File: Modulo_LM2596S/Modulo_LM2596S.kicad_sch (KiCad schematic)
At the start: 17 parts, among them J101 Conn_01x01_Female, J102 Conn_01x01_Female, J103 Conn_01x01_Female, J104 Conn_01x01_Female, U101 LM2596S-ADJ

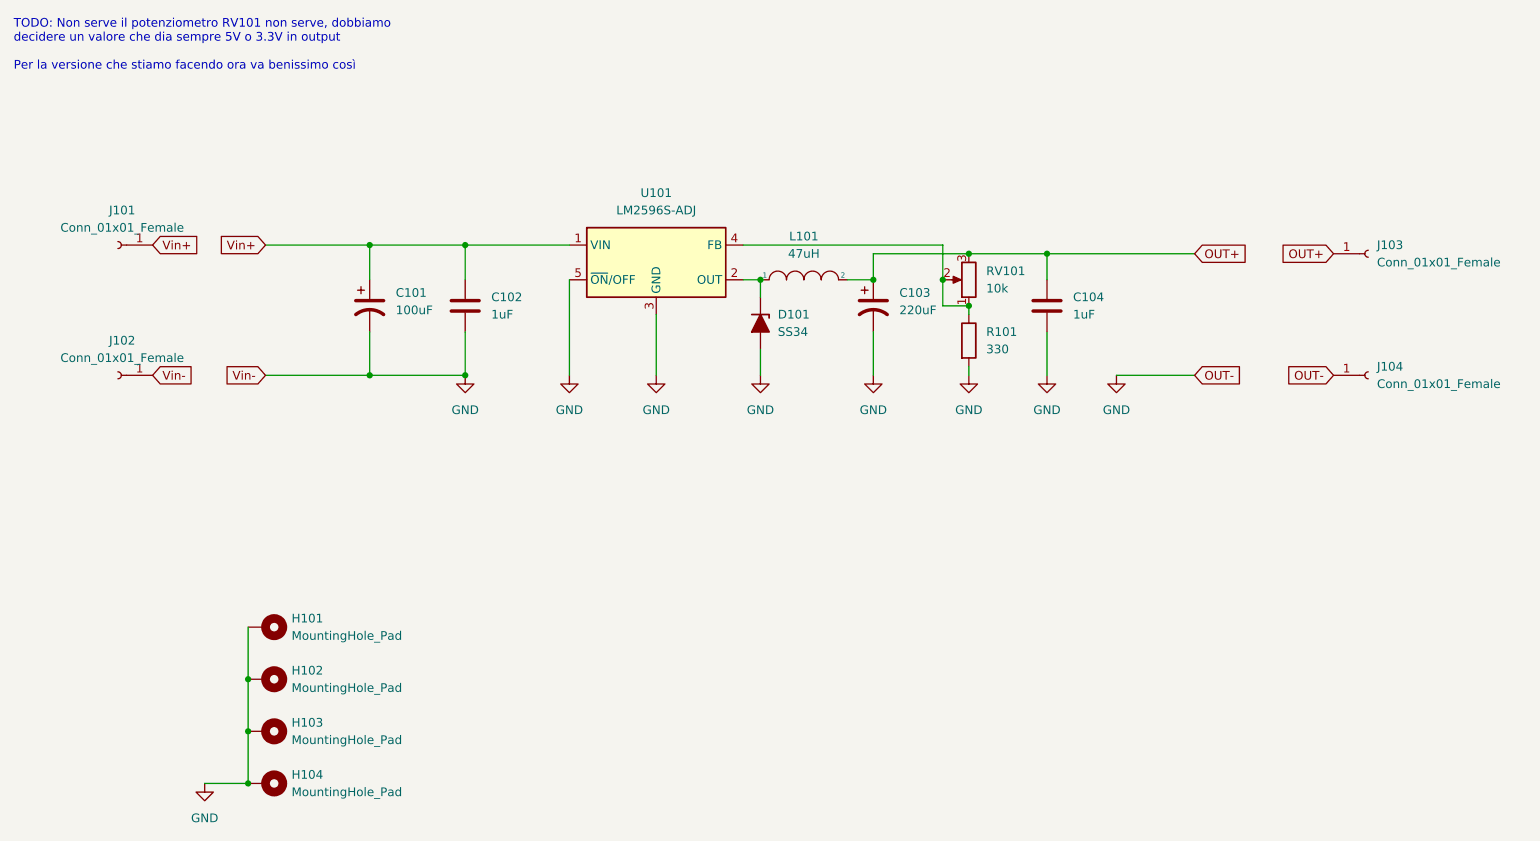
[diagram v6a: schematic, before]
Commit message: LM2596S: Creazione del layout e inserimento dei solderpoints
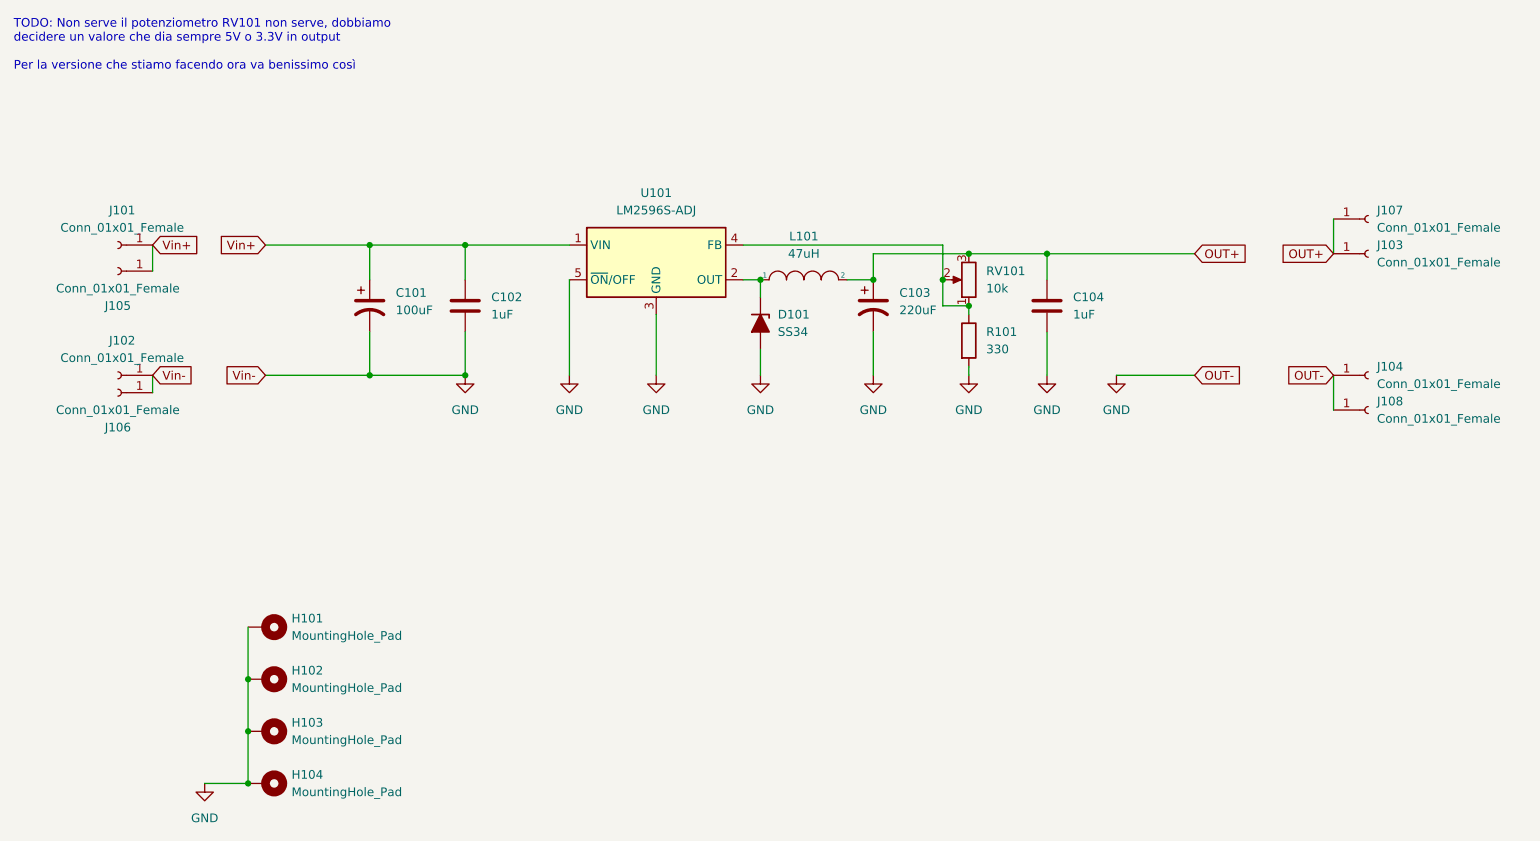
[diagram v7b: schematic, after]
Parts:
- added J105, J106, J107, J108: Conn_01x01_Female, Connector_Wire:SolderWirePad_1x01_SMD_1x2mm, symbol Connector:Conn_01x01_Female
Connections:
- net GND: now also J106.1 (Pin_1), J108.1 (Pin_1)
- net OUT+: now also J107.1 (Pin_1)
- net Vin+: now also J105.1 (Pin_1)
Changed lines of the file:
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@@
+    (stroke (width 0) (type default) (color 0 0 0 0))
+  )
+  (wire (pts (xy 213.36 68.58) (xy 213.36 73.66))
     (stroke (width 0) (type default) (color 0 0 0 0))
   )
@@
     (stroke (width 0) (type default) (color 0 0 0 0))
   )
+  (wire (pts (xy 40.64 91.44) (xy 40.64 93.98))
+    (stroke (width 0) (type default) (color 0 0 0 0))
+  )
   (wire (pts (xy 171.45 73.66) (xy 160.02 73.66))
     (stroke (width 0) (type default) (color 0 0 0 0))
@@
     (stroke (width 0) (type default) (color 0 0 0 0))
   )
+  (wire (pts (xy 40.64 72.39) (xy 40.64 76.2))
+    (stroke (width 0) (type default) (color 0 0 0 0))
+  )
   (wire (pts (xy 160.02 81.28) (xy 160.02 82.55))
     (stroke (width 0) (type default) (color 0 0 0 0))
@@
   )
   (wire (pts (xy 127 77.47) (xy 129.54 77.47))
+    (stroke (width 0) (type default) (color 0 0 0 0))
+  )
+  (wire (pts (xy 213.36 91.44) (xy 213.36 96.52))
     (stroke (width 0) (type default) (color 0 0 0 0))
   )
@@
     (pin "1")
   )
+  (symbol (lib_id "Connector:Conn_01x01_Female") (at 218.44 96.52 0) (unit 1)
+    (in_bom yes) (on_board yes) (fields_autoplaced)
+    (property "Reference" "J108" (id 0) (at 219.71 95.2499 0)
+      (effects (font (size 1.27 1.27)) (justify left))
+    )
+    (property "Value" "Conn_01x01_Female" (id 1) (at 219.71 97.7899 0)
+      (effects (font (size 1.27 1.27)) (justify left))
+    )
+    (property "Footprint" "Connector_Wire:SolderWirePad_1x01_SMD_1x2mm" (id 2) (at 218.44 96.52 0)
+      (effects (font (size 1.27 1.27)) hide)
+    )
+    (property "Datasheet" "~" (id 3) (at 218.44 96.52 0)
+      (effects (font (size 1.27 1.27)) hide)
+    )
+    (pin "1")
+  )
   (symbol (lib_id "Mechanical:MountingHole_Pad") (at 57.15 128.27 270) (unit 1)
     (in_bom yes) (on_board yes) (fields_autoplaced)
@@
     (pin "1")
   )
+  (symbol (lib_id "Connector:Conn_01x01_Female") (at 35.56 76.2 180) (unit 1)
+    (in_bom yes) (on_board yes)
+    (property "Reference" "J105" (id 0) (at 35.56 81.28 0))
+    (property "Value" "Conn_01x01_Female" (id 1) (at 35.56 78.74 0))
+    (property "Footprint" "Connector_Wire:SolderWirePad_1x01_SMD_1x2mm" (id 2) (at 35.56 76.2 0)
+      (effects (font (size 1.27 1.27)) hide)
+    )
+    (property "Datasheet" "~" (id 3) (at 35.56 76.2 0)
+      (effects (font (size 1.27 1.27)) hide)
+    )
+    (pin "1")
+  )
   (symbol (lib_id "Mechanical:MountingHole_Pad") (at 57.15 151.13 270) (unit 1)
     (in_bom yes) (on_board yes) (fields_autoplaced)
@@
     (pin "2")
   )
+  (symbol (lib_id "Connector:Conn_01x01_Female") (at 218.44 68.58 0) (unit 1)
+    (in_bom yes) (on_board yes) (fields_autoplaced)
+    (property "Reference" "J107" (id 0) (at 219.71 67.3099 0)
+      (effects (font (size 1.27 1.27)) (justify left))
+    )
+    (property "Value" "Conn_01x01_Female" (id 1) (at 219.71 69.8499 0)
+      (effects (font (size 1.27 1.27)) (justify left))
+    )
+    (property "Footprint" "Connector_Wire:SolderWirePad_1x01_SMD_1x2mm" (id 2) (at 218.44 68.58 0)
+      (effects (font (size 1.27 1.27)) hide)
+    )
+    (property "Datasheet" "~" (id 3) (at 218.44 68.58 0)
+      (effects (font (size 1.27 1.27)) hide)
+    )
+    (pin "1")
+  )
   (symbol (lib_id "Device:R_Potentiometer") (at 160.02 77.47 180) (unit 1)
     (in_bom yes) (on_board yes) (fields_autoplaced)
@@
     (pin "3")
   )
+  (symbol (lib_id "Connector:Conn_01x01_Female") (at 35.56 93.98 180) (unit 1)
+    (in_bom yes) (on_board yes)
+    (property "Reference" "J106" (id 0) (at 35.56 99.06 0))
+    (property "Value" "Conn_01x01_Female" (id 1) (at 35.56 96.52 0))
+    (property "Footprint" "Connector_Wire:SolderWirePad_1x01_SMD_1x2mm" (id 2) (at 35.56 93.98 0)
+      (effects (font (size 1.27 1.27)) hide)
+    )
+    (property "Datasheet" "~" (id 3) (at 35.56 93.98 0)
+      (effects (font (size 1.27 1.27)) hide)
+    )
+    (pin "1")
+  )
   (symbol (lib_id "Connector:Conn_01x01_Female") (at 35.56 91.44 180) (unit 1)
-    (in_bom yes) (on_board yes) (fields_autoplaced)
+    (in_bom yes) (on_board yes)
     (property "Reference" "J102" (id 0) (at 36.195 86.36 0))
     (property "Value" "Conn_01x01_Female" (id 1) (at 36.195 88.9 0))
@@
       (reference "J104") (unit 1) (value "Conn_01x01_Female") (footprint "Connector_Wire:SolderWirePad_1x01_SMD_1x2mm")
     )
+    (path "/51228ca2-a49a-4b15-9ded-c4c970287008"
+      (reference "J105") (unit 1) (value "Conn_01x01_Female") (footprint "Connector_Wire:SolderWirePad_1x01_SMD_1x2mm")
+    )
+    (path "/e362e41a-53c4-4079-b053-23e78bfaa3ed"
+      (reference "J106") (unit 1) (value "Conn_01x01_Female") (footprint "Connector_Wire:SolderWirePad_1x01_SMD_1x2mm")
+    )
+    (path "/ad1d5605-c410-4b2c-a700-5ce4c68c5394"
+      (reference "J107") (unit 1) (value "Conn_01x01_Female") (footprint "Connector_Wire:SolderWirePad_1x01_SMD_1x2mm")
+    )
+    (path "/0fad0d52-c86b-429f-9273-4dd1d7506cb5"
+      (reference "J108") (unit 1) (value "Conn_01x01_Female") (footprint "Connector_Wire:SolderWirePad_1x01_SMD_1x2mm")
+    )
     (path "/6d551d3c-151e-4aa5-b2c4-444cfcec29b2"
